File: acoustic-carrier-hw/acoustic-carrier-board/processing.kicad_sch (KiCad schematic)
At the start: 24 parts, among them IC1 ECP5-BGA256, J4 Conn_01x06_Socket, J8 Conn_01x06_Socket, U4 W25Q128JVS, U9 W25Q128JVS

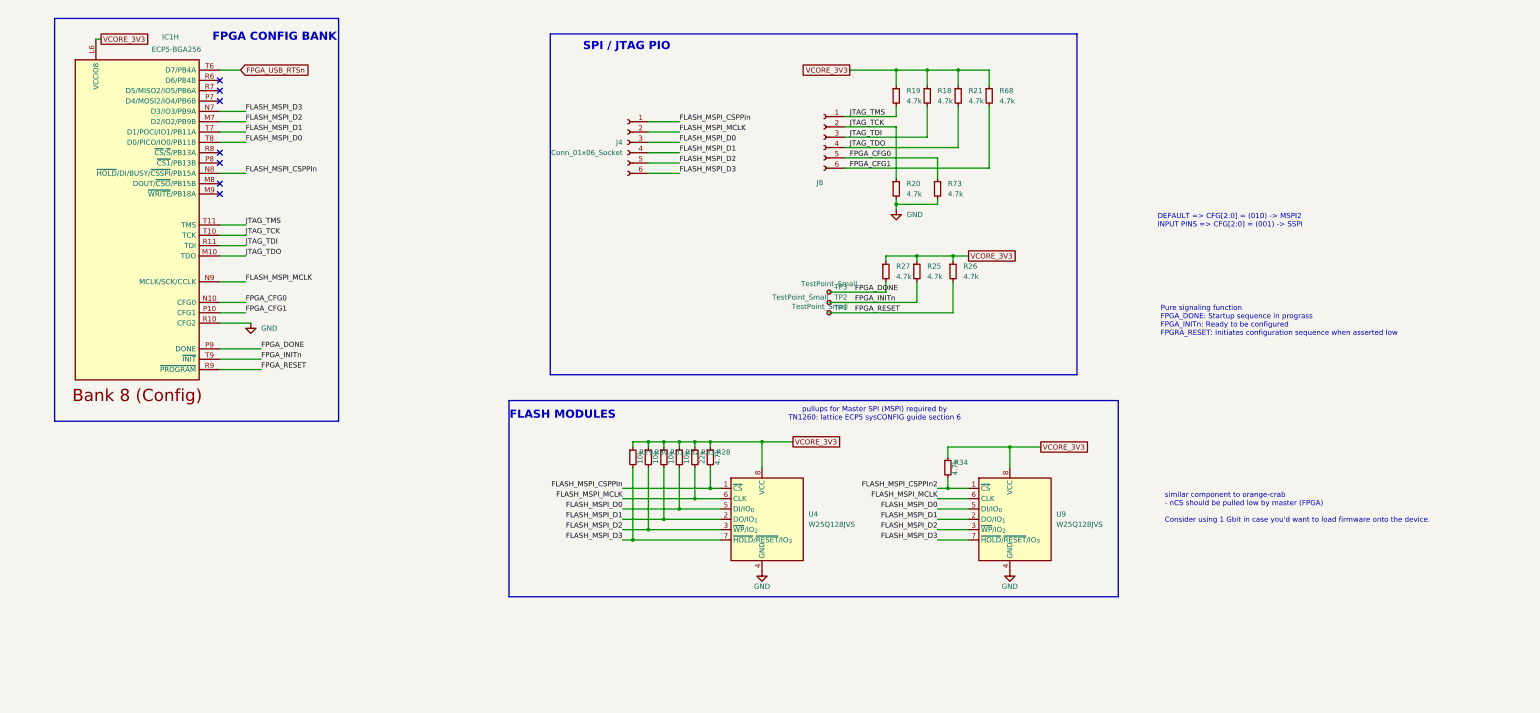
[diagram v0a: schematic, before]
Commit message: [carrier] Finished flash and config check
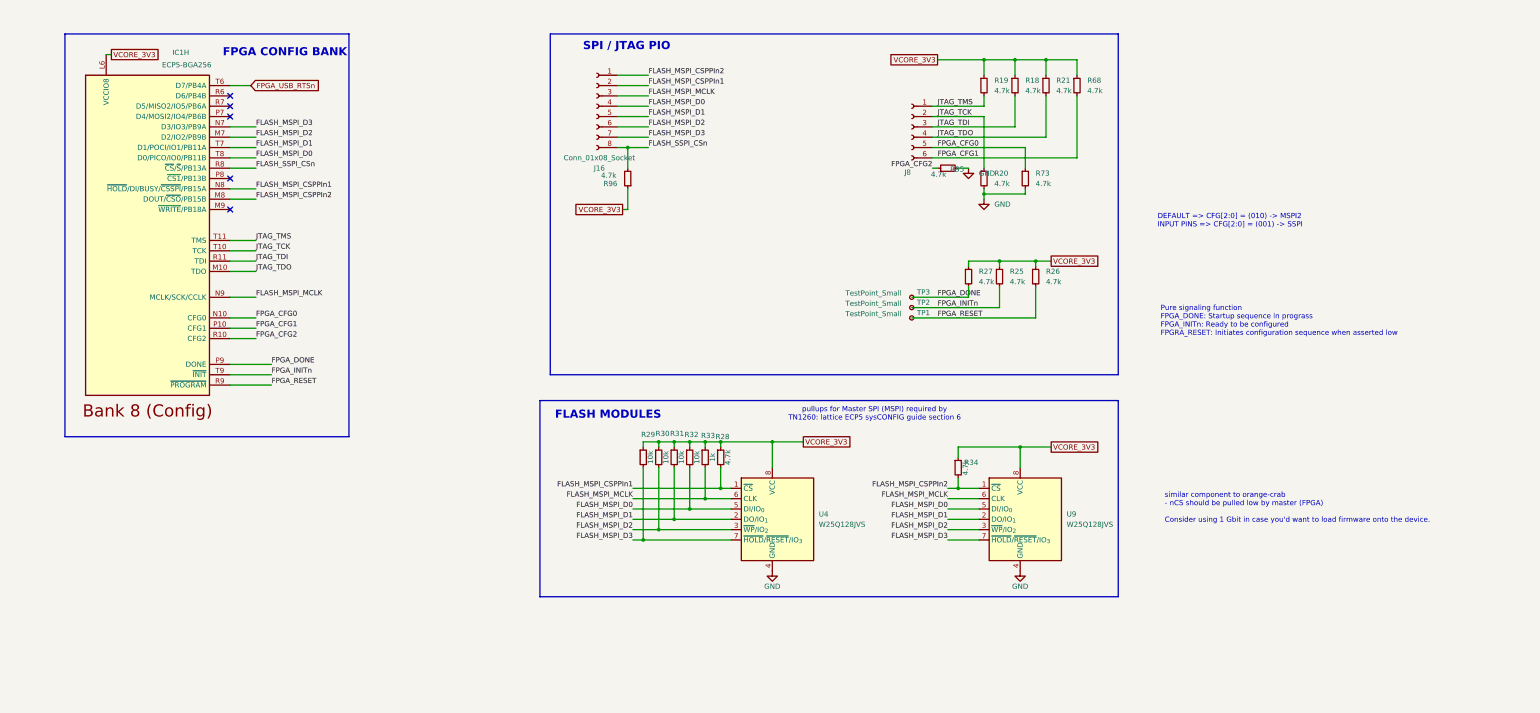
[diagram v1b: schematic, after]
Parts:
- removed J4: Conn_01x06_Socket, Connector_PinHeader_1.27mm:PinHeader_1x06_P1.27mm_Vertical, symbol Connector:Conn_01x06_Socket
- added J16: Conn_01x08_Socket, symbol Connector:Conn_01x08_Socket
- added R95, R96: 4.7k, Resistor_SMD:R_0402_1005Metric, symbol Device:R_Small
- R33: value 22k -> 1k; LPN C25768 -> C11702; MPN 0402WGF2202TCE -> 0402WGF1001TCE
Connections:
- net FLASH_MSPI_CSPPIn2: now also IC1.M8 (DOUT/~{CSO}/PB15B), J16.1 (Pin_1)
- net FLASH_MSPI_D0: now also J16.4 (Pin_4)
- net FLASH_MSPI_D1: now also J16.5 (Pin_5)
- net FLASH_MSPI_D2: now also J16.6 (Pin_6)
- net FLASH_MSPI_D3: now also J16.7 (Pin_7)
- net FLASH_MSPI_MCLK: now also J16.3 (Pin_3)
- net GND: now also R95.2; no longer IC1.R10 (CFG2)
- net VCORE_3V3: now also R96.1
- net FLASH_SSPI_CSn: now reaches IC1.R8 (~{CS}/~{S}/PB13A)
- net FLASH_SSPI_CSn: now also J16.8 (Pin_8), R96.2
- net FLASH_MSPI_CSPPIn renamed FLASH_MSPI_CSPPIn1
- net FLASH_MSPI_CSPPIn1: now also J16.2 (Pin_2)
- new net FPGA_CFG2: IC1.R10 (CFG2), R95.1
- no-connect marks 7 -> 5
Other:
- moved on the sheet: IC1H, J8, R18, R19, R20, R21, R25, R26, R27, R28, R29, R30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

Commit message: [carrier] Reorganized schematic, moPut adc signals in bus, fixed DRC errors (next) recheck ethernet, check usb, add power switch
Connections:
- net FPGA_USB_RTSn: no longer names the net of IC1.T6 (D7/PB4A)
- no-connect marks 5 -> 6
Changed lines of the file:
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@@
+	)
+	(no_connect
+		(at 59.69 33.02)
 	)
 	(no_connect
@@
 		(pts
 			(xy 168.91 120.65) (xy 168.91 121.92)
-		)
-		(stroke
-			(width 0)
-			(type default)
-		)
-	)
-	(wire
-		(pts
-			(xy 59.69 33.02) (xy 64.77 33.02)
 		)
 		(stroke
@@
 			(effects
 				(font
-					(size 1.27 1.27)
-				)
-				(justify left)
-				(hide yes)
-			)
-		)
-	)
-	(global_label "FPGA_USB_RTSn"
-		(shape input)
-		(at 64.77 33.02 0)
-		(fields_autoplaced yes)
-		(effects
-			(font
-				(size 1.27 1.27)
-			)
-			(justify left)
-		)
-		(property "Intersheetrefs" "${INTERSHEET_REFS}"
-			(at 82.8137 33.02 0)
-			(effects
-				(font

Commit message: [carrier] Fixed error in ethernet power supply, separated footprints + symbols into library (next) check whether supply should be DVDDH
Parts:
- removed IC1: ECP5-BGA256, fpga:BGA256C80P16X16_1400X1400X170, symbol ecp5bga256:ECP5-BGA256
- added IC1: ECP5-BGA256, iw-fpga_mcu:BGA256C80P16X16_1400X1400X170, symbol iw-fpga_mcu:ECP5-BGA256
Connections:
- net FLASH_MSPI_CSPPIn1: now also IC1.N8 (~{HOLD}/DI/BUSY/~{CSSPI}/PB15A)
- net FLASH_MSPI_CSPPIn2: now also IC1.M8 (DOUT/~{CSO}/PB15B)
- net FLASH_MSPI_D0: now also IC1.T8 (D0/PICO/IO0/PB11B)
- net FLASH_MSPI_D1: now also IC1.T7 (D1/POCI/IO1/PB11A)
- net FLASH_MSPI_D2: now also IC1.M7 (D2/IO2/PB9B)
- net FLASH_MSPI_D3: now also IC1.N7 (D3/IO3/PB9A)
- net FLASH_MSPI_MCLK: now also IC1.N9 (MCLK/SCK/CCLK)
- net FLASH_SSPI_CSn: now also IC1.R8 (~{CS}/~{S}/PB13A)
- net FPGA_CFG0: now also IC1.N10 (CFG0)
- net FPGA_CFG1: now also IC1.P10 (CFG1)
- net FPGA_CFG2: now also IC1.R10 (CFG2)
- net FPGA_DONE: now also IC1.P9 (DONE)
- net FPGA_INITn: now also IC1.T9 (~{INIT})
- net FPGA_RESET: now also IC1.R9 (~{PROGRAM})
- net JTAG_TCK: now also IC1.T10 (TCK)
- net JTAG_TDI: now also IC1.R11 (TDI)
- net JTAG_TDO: now also IC1.M10 (TDO)
- net JTAG_TMS: now also IC1.T11 (TMS)
- net VCORE_3V3: now also IC1.L6 (VCCIO8)

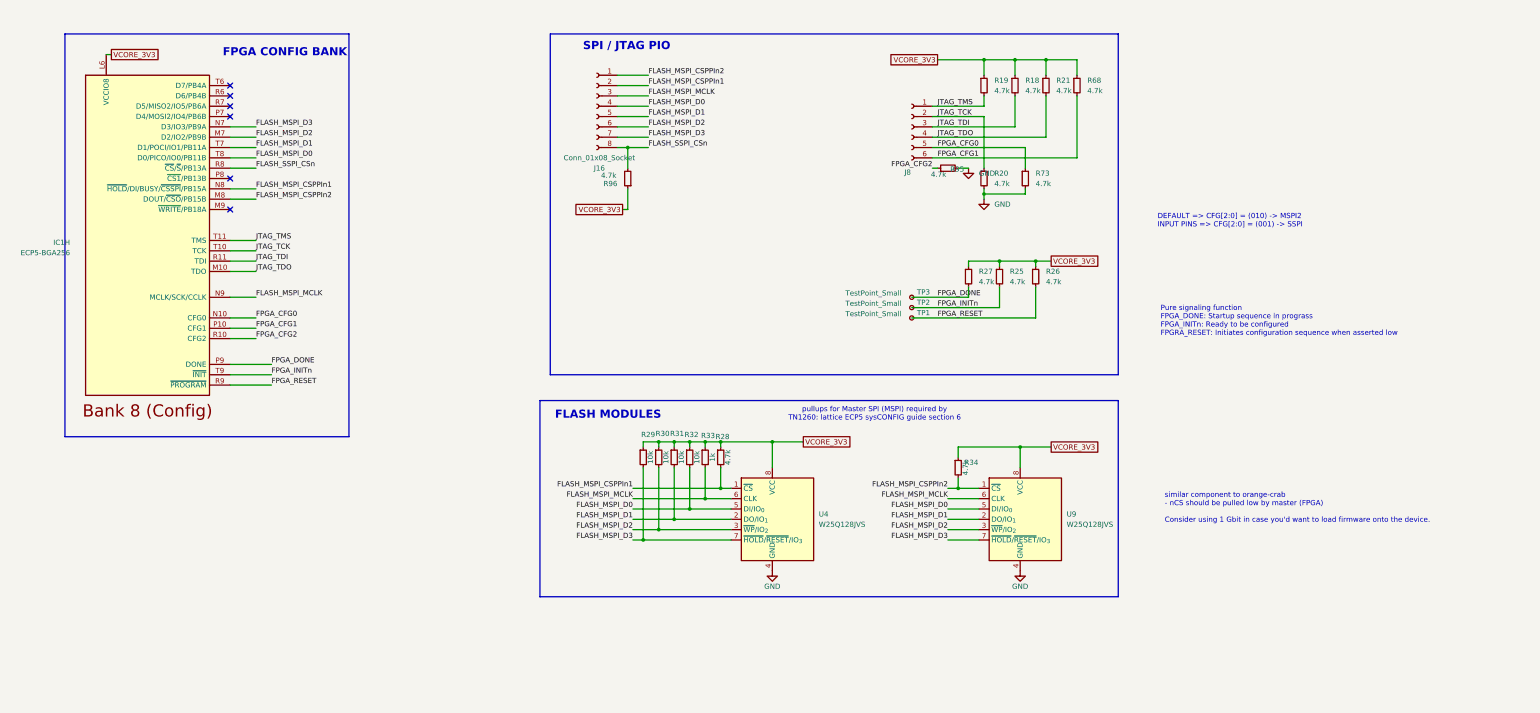
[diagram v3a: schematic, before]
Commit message: [carrier] Signal switch-around in ddr3
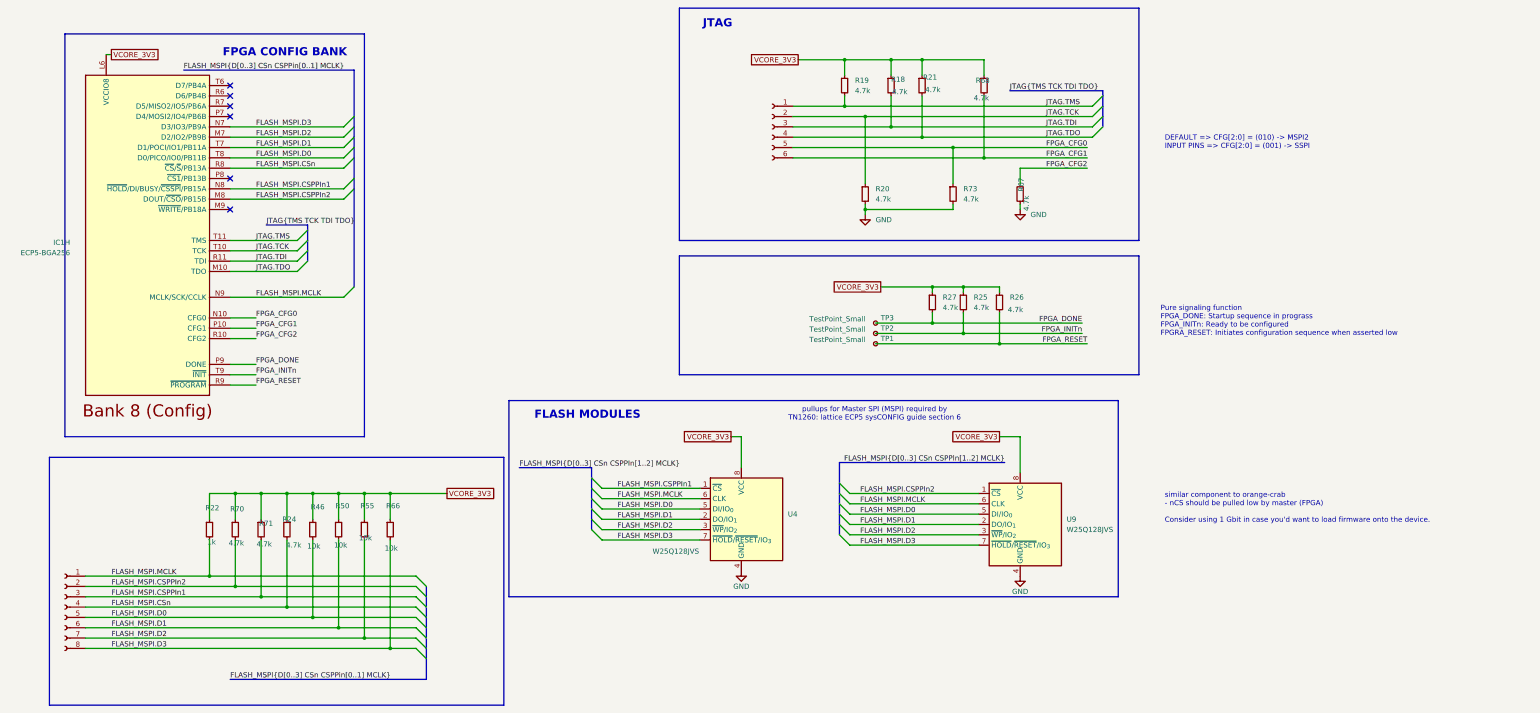
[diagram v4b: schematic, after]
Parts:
- removed R28, R34, R95, R96: 4.7k, Resistor_SMD:R_0402_1005Metric, symbol Device:R_Small
- removed R29, R30, R31, R32: 10k, Resistor_SMD:R_0402_1005Metric, symbol Device:R_Small
- removed R33: 1k, Resistor_SMD:R_0402_1005Metric, symbol Device:R_Small
- added R22: 1k, Resistor_SMD:R_0402_1005Metric, symbol Device:R_Small
- added R24, R67, R70, R71: 4.7k, Resistor_SMD:R_0402_1005Metric, symbol Device:R_Small
- added R46, R50, R55, R66: 10k, Resistor_SMD:R_0402_1005Metric, symbol Device:R_Small
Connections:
- net FPGA_CFG2: now also R67.2
- net GND: now also R67.1
- net VCORE_3V3: now also R22.1, R24.1, R46.1, R50.1, R55.1, R66.1, R70.1, R71.1
- net FLASH_MSPI_CSPPIn1 renamed FLASH_MSPI.CSPPIn1
- net FLASH_MSPI.CSPPIn1: now also J16.3 (Pin_3), R71.2; no longer J16.2 (Pin_2)
- net FLASH_MSPI_CSPPIn2 renamed FLASH_MSPI.CSPPIn2
- net FLASH_MSPI.CSPPIn2: now also J16.2 (Pin_2), R70.2; no longer J16.1 (Pin_1)
- net FLASH_MSPI_D0 renamed FLASH_MSPI.D0
- net FLASH_MSPI.D0: now also J16.5 (Pin_5), R46.2; no longer J16.4 (Pin_4)
- net FLASH_MSPI_D1 renamed FLASH_MSPI.D1
- net FLASH_MSPI.D1: now also J16.6 (Pin_6), R50.2; no longer J16.5 (Pin_5)
- net FLASH_MSPI_D2 renamed FLASH_MSPI.D2
- net FLASH_MSPI.D2: now also J16.7 (Pin_7), R55.2; no longer J16.6 (Pin_6)
- net FLASH_MSPI_D3 renamed FLASH_MSPI.D3
- net FLASH_MSPI.D3: now also J16.8 (Pin_8), R66.2; no longer J16.7 (Pin_7)
- net FLASH_MSPI_MCLK renamed FLASH_MSPI.MCLK
- net FLASH_MSPI.MCLK: now also J16.1 (Pin_1), R22.2; no longer J16.3 (Pin_3)
- net FLASH_SSPI_CSn renamed FLASH_MSPI.CSn
- net FLASH_MSPI.CSn: now also J16.4 (Pin_4), R24.2; no longer J16.8 (Pin_8)
- net JTAG_TCK renamed JTAG.TCK
- net JTAG_TDI renamed JTAG.TDI
- net JTAG_TDO renamed JTAG.TDO
- net JTAG_TMS renamed JTAG.TMS
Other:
- note added: "JTAG"
- note removed: "SPI / JTAG PIO"
- moved on the sheet: R18, R19, R20, R21, R25, R26, R27, R68, R73, TP1, TP2, TP3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

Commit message: [¢arrier] Fixed busses, added resistive arrays instead of 4x4k7 or 4x10k
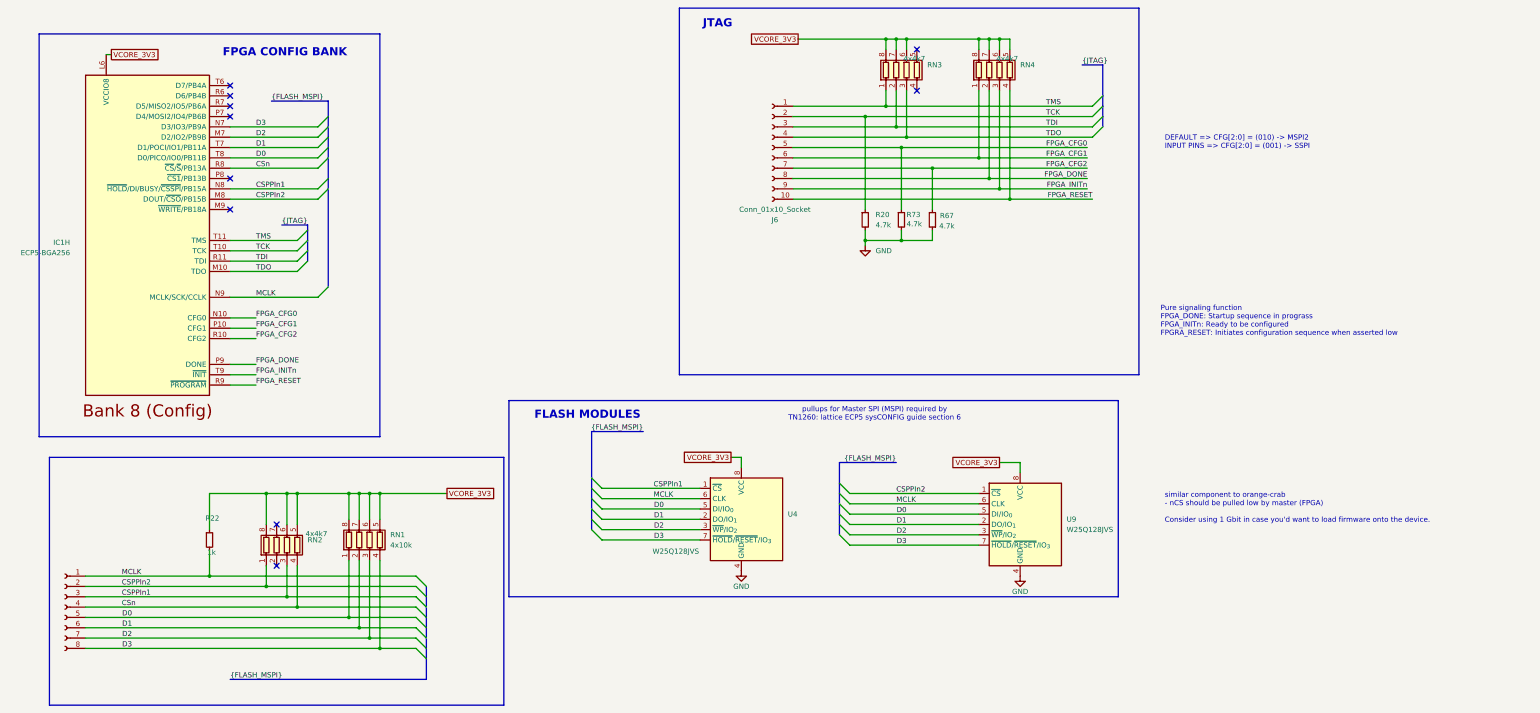
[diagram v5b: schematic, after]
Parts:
- removed J8: Conn_01x06_Socket, Connector_PinHeader_1.27mm:PinHeader_1x06_P1.27mm_Vertical, symbol Connector:Conn_01x06_Socket
- removed R18, R19, R21, R24, R25, R26, R27, R68, R70, R71: 4.7k, Resistor_SMD:R_0402_1005Metric, symbol Device:R_Small
- removed R46, R50, R55, R66: 10k, Resistor_SMD:R_0402_1005Metric, symbol Device:R_Small
- removed TP1, TP2, TP3: TestPoint_Small, TestPoint:TestPoint_Pad_D1.5mm, symbol Connector:TestPoint_Small
- added J6: Conn_01x10_Socket, symbol Connector:Conn_01x10_Socket
- added RN1: 4x10k, Resistor_SMD:R_Array_Convex_4x0603, symbol Device:R_Pack04
- added RN2, RN3, RN4: 4x4k7, Resistor_SMD:R_Array_Convex_4x0603, symbol Device:R_Pack04
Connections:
- net FPGA_CFG0: now also J6.5 (Pin_5)
- net FPGA_CFG1: now also J6.6 (Pin_6), RN4.1 (R1.1)
- net FPGA_CFG2: now also J6.7 (Pin_7)
- net FPGA_DONE: now also J6.8 (Pin_8), RN4.2 (R2.1)
- net FPGA_INITn: now also J6.9 (Pin_9), RN4.3 (R3.1)
- net FPGA_RESET: now also J6.10 (Pin_10), RN4.4 (R4.1)
- net VCORE_3V3: now also RN1.5 (R4.2), RN1.6 (R3.2), RN1.7 (R2.2), RN1.8 (R1.2), RN2.5 (R4.2), RN2.6 (R3.2), RN2.8 (R1.2), RN3.6 (R3.2), RN3.7 (R2.2), RN3.8 (R1.2), RN4.5 (R4.2), RN4.6 (R3.2), RN4.7 (R2.2), RN4.8 (R1.2)
- net FLASH_MSPI.CSPPIn1 renamed CSPPIn1
- net CSPPIn1: now also RN2.3 (R3.1)
- net FLASH_MSPI.CSPPIn2 renamed CSPPIn2
- net CSPPIn2: now also RN2.1 (R1.1)
- net FLASH_MSPI.CSn renamed CSn
- net CSn: now also RN2.4 (R4.1)
- net FLASH_MSPI.D0 renamed D0
- net D0: now also RN1.1 (R1.1)
- net FLASH_MSPI.D1 renamed D1
- net D1: now also RN1.2 (R2.1)
- net FLASH_MSPI.D2 renamed D2
- net D2: now also RN1.3 (R3.1)
- net FLASH_MSPI.D3 renamed D3
- net D3: now also RN1.4 (R4.1)
- net FLASH_MSPI.MCLK renamed MCLK
- net JTAG.TCK renamed TCK
- net TCK: now also J6.2 (Pin_2)
- net JTAG.TDI renamed TDI
- net TDI: now also J6.3 (Pin_3), RN3.2 (R2.1)
- net JTAG.TDO renamed TDO
- net TDO: now also J6.4 (Pin_4), RN3.3 (R3.1)
- net JTAG.TMS renamed TMS
- net TMS: now also J6.1 (Pin_1), RN3.1 (R1.1)
- no-connect marks 6 -> 10
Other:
- moved on the sheet: R20, R22, R67, R73
